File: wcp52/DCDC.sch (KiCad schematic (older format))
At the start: 55 parts, among them Q15 MMBT3904, Q16 MMBT3904, Q17 PZT2907A, Q18 PZT2907A, Q19 MMBT3904, Q20 MMBT3904, U13 L78M05CDT, U14 MC79M05CDT, U15 AZ1117CH-1.8TRG1, U16 MCP1700T-3302E/TT

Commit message: Prepare to fab
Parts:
- added R117: 360, IPC7351-Nominal:RESC1608X50, symbol R-0603
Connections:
- net GND: now also R117.1
- net OUT+1V8: now also R117.2

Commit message: BOM line fixes
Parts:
- C76, C77, C82, C83: Description (none) -> CAP ALU-POLY 100uF 16V
- C78, C79, C80, C81, C84, C85, C86, C87, C88, C89, C90, C91, C92, C93, D7, D8, Q15, Q16, Q19, Q20, R117, R89, R90, R91, R92, R93, R94, R95, R96, R98, R99: Manuf Value -> (none)
- L10, L8, L9: Description (none) -> IND CHIP 4.7uH 300mA [0805]
- L6, L7: Description (none) -> IND WOUND 220uH 700mA
- R97: Description (none) -> PPTC 100mA/250mA 60V [1206]

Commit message: BOM corrections/combinations, etc
Add configuration for bomtool
Remove old schematic file no longer used
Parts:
- DZ10: BOM (none) -> SEMI GENERIC BZX84C10
- DZ9: BOM (none) -> SEMI GENERIC BZX84C3V9
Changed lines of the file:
@@
 F 2 "smd-semi:SOT-23" H 5250 2700 50  0001 C CNN
 F 3 "" H 5250 2700 60  0000 C CNN
-F 4 "DZ9" H 5250 2700 50  0001 C CNN "OldReference"
+F 4 "SEMI GENERIC BZX84C10" H 5250 2700 60  0001 C CNN "BOM"
+F 5 "DZ9" H 5250 2700 50  0001 C CNN "OldReference"
 	1    5250 2700
 	1    0    0    -1
@@
 F 2 "smd-semi:SOT-23" H 4750 5100 50  0001 C CNN
 F 3 "" H 4750 5100 60  0000 C CNN
-F 4 "DZ11" H 4750 5100 50  0001 C CNN "OldReference"
+F 4 "SEMI GENERIC BZX84C3V9" H 4750 5100 60  0001 C CNN "BOM"
+F 5 "DZ11" H 4750 5100 50  0001 C CNN "OldReference"
 	1    4750 5100
 	1    0    0    -1

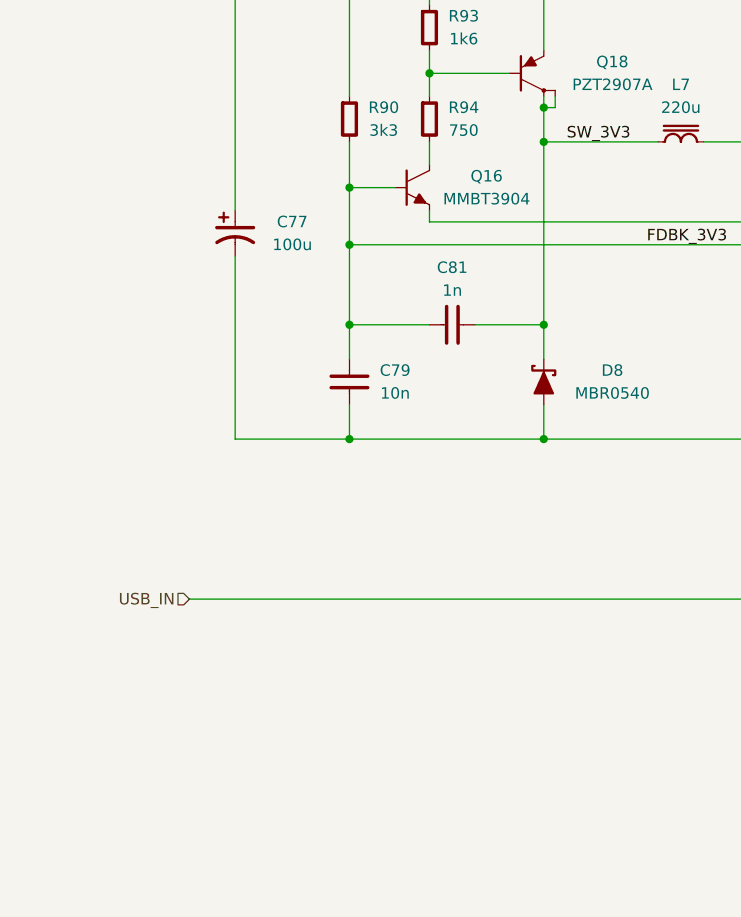
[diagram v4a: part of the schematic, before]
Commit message: Schematic updates for documentation
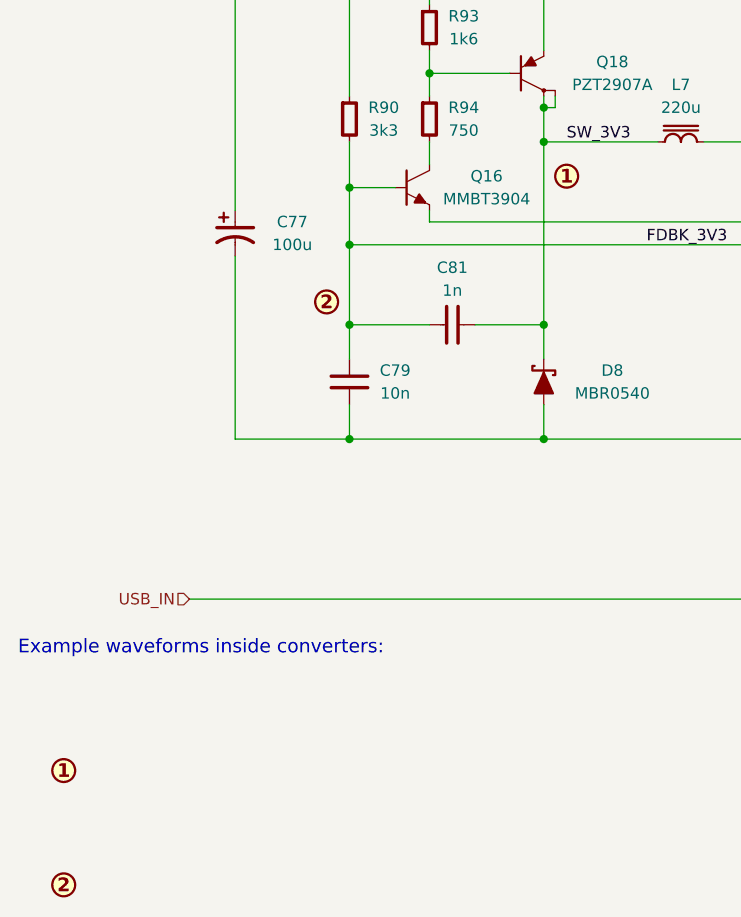
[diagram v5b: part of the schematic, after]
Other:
- note added: "Example waveforms inside converters:"

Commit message: More doc fixes
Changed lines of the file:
@@
 U 1 1 54F4E82D
 P 2300 1900
-F 0 "Q15" H 2600 1950 50  0000 C CNN
-F 1 "MMBT3904" H 2600 1850 50  0000 C CNN
+F 0 "Q15" H 2450 1900 50  0000 C CNN
+F 1 "MMBT3904" H 2600 1850 50  0001 C CNN
 F 2 "smd-semi:SOT-23" H 2300 1900 50  0001 C CNN
 F 3 "" H 2300 1900 60  0000 C CNN
@@
 U 1 1 54F4F95D
 P 4150 1400
-F 0 "Q19" H 4450 1450 50  0000 C CNN
-F 1 "MMBT3904" H 4450 1350 50  0000 C CNN
+F 0 "Q19" H 4300 1400 50  0000 C CNN
+F 1 "MMBT3904" H 4450 1350 50  0001 C CNN
 F 2 "smd-semi:SOT-23" H 4150 1400 50  0001 C CNN
 F 3 "" H 4150 1400 60  0000 C CNN
@@
 U 1 1 54F53F97
 P 2300 4300
-F 0 "Q16" H 2600 4350 50  0000 C CNN
-F 1 "MMBT3904" H 2600 4250 50  0000 C CNN
+F 0 "Q16" H 2450 4300 50  0000 C CNN
+F 1 "MMBT3904" H 2600 4250 50  0001 C CNN
 F 2 "smd-semi:SOT-23" H 2300 4300 50  0001 C CNN
 F 3 "" H 2300 4300 60  0000 C CNN
@@
 U 1 1 54F53FF2
 P 4150 3800
-F 0 "Q20" H 4450 3850 50  0000 C CNN
-F 1 "MMBT3904" H 4450 3750 50  0000 C CNN
+F 0 "Q20" H 4300 3800 50  0000 C CNN
+F 1 "MMBT3904" H 4450 3750 50  0001 C CNN
 F 2 "smd-semi:SOT-23" H 4150 3800 50  0001 C CNN
 F 3 "" H 4150 3800 60  0000 C CNN
@@
 Example waveforms inside converters:
 $Comp
-L N1 #SYM75
+L N1 #SYM85
 U 1 1 550EB3FC
 P 2950 4250
-F 0 "#SYM75" H 2950 4250 60  0001 C CNN
+F 0 "#SYM85" H 2950 4250 60  0001 C CNN
 F 1 "N1" H 2950 4250 60  0001 C CNN
 F 2 "" H 2950 4250 60  0000 C CNN
@@
 $EndComp
 $Comp
-L N2 #SYM74
+L N2 #SYM84
 U 1 1 550EB574
 P 1900 4800
-F 0 "#SYM74" H 1900 4800 60  0001 C CNN
+F 0 "#SYM84" H 1900 4800 60  0001 C CNN
 F 1 "N2" H 1900 4800 60  0001 C CNN
 F 2 "" H 1900 4800 60  0000 C CNN
@@
 $EndComp
 $Comp
-L N1 #SYM72
+L N1 #SYM82
 U 1 1 550EB5F6
 P 750 6850
-F 0 "#SYM72" H 750 6850 60  0001 C CNN
+F 0 "#SYM82" H 750 6850 60  0001 C CNN
 F 1 "N1" H 750 6850 60  0001 C CNN
 F 2 "" H 750 6850 60  0000 C CNN
@@
 $EndComp
 $Comp
-L N2 #SYM73
+L N2 #SYM83
 U 1 1 550EBB41
 P 750 7350
-F 0 "#SYM73" H 750 7350 60  0001 C CNN
+F 0 "#SYM83" H 750 7350 60  0001 C CNN
 F 1 "N2" H 750 7350 60  0001 C CNN
 F 2 "" H 750 7350 60  0000 C CNN

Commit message: Nicer BOM lines
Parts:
- C76: OldReference C96 -> (none)
- C77: OldReference C97 -> (none)
- C78: OldReference C61 -> (none)
- C79: OldReference C62 -> (none)
- C80: OldReference C68 -> (none)
- C81: OldReference C73 -> (none)
- C82: OldReference C100 -> (none)
- C83: OldReference C101 -> (none)
- C84: OldReference C102 -> (none)
- C85: OldReference C103 -> (none)
- C86: OldReference C104 -> (none)
- C87: OldReference C105 -> (none)
- C88: OldReference C106 -> (none)
- C89: OldReference C107 -> (none)
- C90: OldReference C112 -> (none)
- C91: OldReference C113 -> (none)
- C92: OldReference C110 -> (none)
- C93: OldReference C111 -> (none)
- D7: BOM SEMI GENERIC MBR0540 -> SCHOTTKY MBR0540; OldReference D3 -> (none)
- D8: BOM SEMI GENERIC MBR0540 -> SCHOTTKY MBR0540; OldReference D4 -> (none)
- DZ10: BOM SEMI GENERIC BZX84C10 -> ZENER BZX84C10; OldReference DZ9 -> (none)
- DZ9: BOM SEMI GENERIC BZX84C3V9 -> ZENER BZX84C3V9; OldReference DZ11 -> (none)
- L10: OldReference L10 -> (none)
- L6: OldReference L6 -> (none)
- L7: OldReference L7 -> (none)
- L8: OldReference L8 -> (none)
- L9: OldReference L9 -> (none)
- Q15: BOM SEMI GENERIC MMBT3904 -> NPN MMBT3904; OldReference Q13 -> (none)
- Q16: BOM SEMI GENERIC MMBT3904 -> NPN MMBT3904; OldReference Q16 -> (none)
- Q17: BOM SEMI GENERIC PZT2907A -> PNP PZT2907A; OldReference Q17 -> (none)
- Q18: BOM SEMI GENERIC PZT2907A -> PNP PZT2907A; OldReference Q18 -> (none)
- Q19: BOM SEMI GENERIC MMBT3904 -> NPN MMBT3904; OldReference Q15 -> (none)
- Q20: BOM SEMI GENERIC MMBT3904 -> NPN MMBT3904; OldReference Q19 -> (none)
- R117: OldReference R23 -> (none)
- R89: OldReference R82 -> (none)
- R90: OldReference R40 -> (none)
- R91: OldReference R65 -> (none)
- R92: OldReference R68 -> (none)
- R93: OldReference R61 -> (none)
- R94: OldReference R63 -> (none)
- R95: OldReference R85 -> (none)
- R96: OldReference R95 -> (none)
- R97: OldReference R96 -> (none)
- R98: OldReference R88 -> (none)
- R99: OldReference R87 -> (none)
- TP10: OldReference TP8 -> (none)
- TP11: OldReference TP9 -> (none)
- TP12: OldReference TP10 -> (none)
- TP13: OldReference TP11 -> (none)
- TP7: OldReference TP5 -> (none)
- TP8: OldReference TP6 -> (none)
- TP9: OldReference TP7 -> (none)
- U13: OldReference U14 -> (none)
- U14: OldReference U15 -> (none)
- U15: OldReference U16 -> (none)
- U16: OldReference U17 -> (none)

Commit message: Add post-testing revision, todo notes
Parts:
- R95, R96: value 1R -> 1R8; BOM RES SMD 1 5% [1210] -> RES SMD 1.8 5% [1210]
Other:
- note added: "TODO (REV 2):\n- C92 could be 2x 10uF, eliminating a BOM item.\n- Can Q17 and Q18 be upgraded to PMOS? In simulation testing\n it was difficult to switch them off quickly and they lost significant\n power. However, the low current gain of the PZT2907A required\n changing the current-limiting resistors to 1R8 and sacrificing output\n current.\n\n Also possible: higher gain BJTs? Darlingtons/Szikla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"
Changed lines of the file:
@@
 Sheet 12 13
 Title "DC-DC Converters"
-Date "2015-03-21"
-Rev ""
+Date "2015-03-31"
+Rev "1"
 Comp "WCP52"
 Comment1 "Gain/Phase Analyzer"
@@
 P 3950 1700
 F 0 "R95" V 3750 1700 50  0000 C CNN
-F 1 "1R" V 3850 1700 50  0000 C CNN
+F 1 "1R8" V 3850 1700 50  0000 C CNN
 F 2 "IPC7351-Nominal:RESC3225X60" H 3950 1700 50  0001 C CNN
 F 3 "" H 3950 1750 60  0000 C CNN
-F 4 "" H 3950 1700 60  0001 C CNN "Manuf"
-F 5 "RES SMD 1 5% [1210]" H 4700 2250 60  0001 C CNN "BOM"
+F 4 "RES SMD 1.8 5% [1210]" H 4700 2250 60  0001 C CNN "BOM"
 	1    3950 1700
 	0    1    1    0
@@
 $EndComp
 $Comp
-L GND #PWR217
+L GND #PWR0215
 U 1 1 54F50066
 P 4900 2500
-F 0 "#PWR217" H 4900 2500 30  0001 C CNN
+F 0 "#PWR0215" H 4900 2500 30  0001 C CNN
 F 1 "GND" H 4900 2430 30  0001 C CNN
 F 2 "" H 4900 2500 60  0000 C CNN
@@
 P 3950 4100
 F 0 "R96" V 3750 4100 50  0000 C CNN
-F 1 "1R" V 3850 4100 50  0000 C CNN
+F 1 "1R8" V 3850 4100 50  0000 C CNN
 F 2 "IPC7351-Nominal:RESC3225X60" H 3950 4100 50  0001 C CNN
 F 3 "" H 3950 4150 60  0000 C CNN
-F 4 "" H 3950 4100 60  0001 C CNN "Manuf"
-F 5 "RES SMD 1 5% [1210]" H 4700 4650 60  0001 C CNN "BOM"
+F 4 "RES SMD 1.8 5% [1210]" H 4700 4650 60  0001 C CNN "BOM"
 	1    3950 4100
 	0    1    1    0
@@
 OUT+3V3
 $Comp
-L GND #PWR216
+L GND #PWR0216
 U 1 1 54F543B2
 P 4750 5500
-F 0 "#PWR216" H 4750 5500 30  0001 C CNN
+F 0 "#PWR0216" H 4750 5500 30  0001 C CNN
 F 1 "GND" H 4750 5430 30  0001 C CNN
 F 2 "" H 4750 5500 60  0000 C CNN
@@
 $EndComp
 $Comp
-L GND #PWR222
+L GND #PWR0217
 U 1 1 54F64B84
 P 6600 1500
-F 0 "#PWR222" H 6600 1500 30  0001 C CNN
+F 0 "#PWR0217" H 6600 1500 30  0001 C CNN
 F 1 "GND" H 6600 1430 30  0001 C CNN
 F 2 "" H 6600 1500 60  0000 C CNN
@@
 $EndComp
 $Comp
-L GND #PWR223
+L GND #PWR0218
 U 1 1 54F676AE
 P 6600 2300
-F 0 "#PWR223" H 6600 2300 30  0001 C CNN
+F 0 "#PWR0218" H 6600 2300 30  0001 C CNN
 F 1 "GND" H 6600 2230 30  0001 C CNN
 F 2 "" H 6600 2300 60  0000 C CNN
@@
 $EndComp
 $Comp
-L GND #PWR218
+L GND #PWR0219
 U 1 1 54F67A48
 P 5900 2350
-F 0 "#PWR218" H 5900 2350 30  0001 C CNN
+F 0 "#PWR0219" H 5900 2350 30  0001 C CNN
 F 1 "GND" H 5900 2280 30  0001 C CNN
 F 2 "" H 5900 2350 60  0000 C CNN
@@
 $EndComp
 $Comp
-L GND #PWR227
+L GND #PWR0220
 U 1 1 54F6971F
 P 7200 2600
-F 0 "#PWR227" H 7200 2600 30  0001 C CNN
+F 0 "#PWR0220" H 7200 2600 30  0001 C CNN
 F 1 "GND" H 7200 2530 30  0001 C CNN
 F 2 "" H 7200 2600 60  0000 C CNN
@@
 $EndComp
 $Comp
-L GND #PWR219
+L GND #PWR0221
 U 1 1 54F6B841
 P 5900 3950
-F 0 "#PWR219" H 5900 3950 30  0001 C CNN
+F 0 "#PWR0221" H 5900 3950 30  0001 C CNN
 F 1 "GND" H 5900 3880 30  0001 C CNN
 F 2 "" H 5900 3950 60  0000 C CNN
@@
 $EndComp
 $Comp
-L GND #PWR228
+L GND #PWR0222
 U 1 1 54F6BEED
 P 7200 4250
-F 0 "#PWR228" H 7200 4250 30  0001 C CNN
+F 0 "#PWR0222" H 7200 4250 30  0001 C CNN
 F 1 "GND" H 7200 4180 30  0001 C CNN
 F 2 "" H 7200 4250 60  0000 C CNN
@@
 $EndComp
 $Comp
-L GND #PWR224
+L GND #PWR0223
 U 1 1 54F6C162
 P 6600 3950
-F 0 "#PWR224" H 6600 3950 30  0001 C CNN
+F 0 "#PWR0223" H 6600 3950 30  0001 C CNN
 F 1 "GND" H 6600 3880 30  0001 C CNN
 F 2 "" H 6600 3950 60  0000 C CNN
@@
 $EndComp
 $Comp
-L GND #PWR220
+L GND #PWR0224
 U 1 1 54F708B6
 P 5900 5550
-F 0 "#PWR220" H 5900 5550 30  0001 C CNN
+F 0 "#PWR0224" H 5900 5550 30  0001 C CNN
 F 1 "GND" H 5900 5480 30  0001 C CNN
 F 2 "" H 5900 5550 60  0000 C CNN
@@
 $EndComp
 $Comp
-L GND #PWR225
+L GND #PWR0225
 U 1 1 54F70A31
 P 6650 5550
-F 0 "#PWR225" H 6650 5550 30  0001 C CNN
+F 0 "#PWR0225" H 6650 5550 30  0001 C CNN
 F 1 "GND" H 6650 5480 30  0001 C CNN
 F 2 "" H 6650 5550 60  0000 C CNN
@@
 $EndComp
 $Comp
-L GND #PWR229
+L GND #PWR0226
 U 1 1 54F71350
 P 7200 5550
-F 0 "#PWR229" H 7200 5550 30  0001 C CNN
+F 0 "#PWR0226" H 7200 5550 30  0001 C CNN
 F 1 "GND" H 7200 5480 30  0001 C CNN
 F 2 "" H 7200 5550 60  0000 C CNN
@@
 $EndComp
 $Comp
-L GND #PWR221
+L GND #PWR0227
 U 1 1 54F777AE
 P 5900 6600
-F 0 "#PWR221" H 5900 6600 30  0001 C CNN
+F 0 "#PWR0227" H 5900 6600 30  0001 C CNN
 F 1 "GND" H 5900 6530 30  0001 C CNN
 F 2 "" H 5900 6600 60  0000 C CNN
@@
 $EndComp
 $Comp
-L GND #PWR226
+L GND #PWR0228
 U 1 1 54F779B8
 P 6650 6600
-F 0 "#PWR226" H 6650 6600 30  0001 C CNN
+F 0 "#PWR0228" H 6650 6600 30  0001 C CNN
 F 1 "GND" H 6650 6530 30  0001 C CNN
 F 2 "" H 6650 6600 60  0000 C CNN
@@
 $EndComp
 $Comp
-L GND #PWR230
+L GND #PWR0229
 U 1 1 54F78198
 P 7200 6600
-F 0 "#PWR230" H 7200 6600 30  0001 C CNN
+F 0 "#PWR0229" H 7200 6600 30  0001 C CNN
 F 1 "GND" H 7200 6530 30  0001 C CNN
 F 2 "" H 7200 6600 60  0000 C CNN
@@
 $EndComp
 $Comp
-L GND #PWR215
+L GND #PWR0230
 U 1 1 54F66084
 P 1500 2250
-F 0 "#PWR215" H 1500 2250 30  0001 C CNN
+F 0 "#PWR0230" H 1500 2250 30  0001 C CNN
 F 1 "GND" H 1500 2180 30  0001 C CNN
 F 2 "" H 1500 2250 60  0000 C CNN
@@
 Connection ~ 7600 5100
 $Comp
-L GND #PWR231
+L GND #PWR0231
 U 1 1 5508DFE8
 P 7600 5550
-F 0 "#PWR231" H 7600 5550 30  0001 C CNN
+F 0 "#PWR0231" H 7600 5550 30  0001 C CNN
 F 1 "GND" H 7600 5480 30  0001 C CNN
 F 2 "" H 7600 5550 60  0000 C CNN
@@
 Example waveforms inside converters:
 $Comp
-L N1 #SYM85
+L N1 #SYM83
 U 1 1 550EB3FC
 P 2950 4250
-F 0 "#SYM85" H 2950 4250 60  0001 C CNN
+F 0 "#SYM83" H 2950 4250 60  0001 C CNN
 F 1 "N1" H 2950 4250 60  0001 C CNN
 F 2 "" H 2950 4250 60  0000 C CNN
@@
 $EndComp
 $Comp
-L N1 #SYM82
+L N1 #SYM85
 U 1 1 550EB5F6
 P 750 6850
-F 0 "#SYM82" H 750 6850 60  0001 C CNN
+F 0 "#SYM85" H 750 6850 60  0001 C CNN
 F 1 "N1" H 750 6850 60  0001 C CNN
 F 2 "" H 750 6850 60  0000 C CNN
@@
 $EndComp
 $Comp
-L N2 #SYM83
+L N2 #SYM86
 U 1 1 550EBB41
 P 750 7350
-F 0 "#SYM83" H 750 7350 60  0001 C CNN
+F 0 "#SYM86" H 750 7350 60  0001 C CNN
 F 1 "N2" H 750 7350 60  0001 C CNN
 F 2 "" H 750 7350 60  0000 C CNN
@@
 	1    0    0    -1
 $EndComp
+Text Notes 3050 7850 0    50   ~ 0
+TODO (REV 2):\n- C92 could be 2x 10uF, eliminating a BOM item.\n- Can Q17 and Q18 be upgraded to PMOS? In simulation testing\n    it was difficult to switch them off quickly and they lost significant\n    power. However, the low current gain of the PZT2907A required\n    changing the current-limiting resistors to 1R8 and sacrificing output\n    current.\n\n    Also possible: higher gain BJTs? Darlingtons/Sziklais? (probably\n    too slow)
 $EndSCHEMATC
